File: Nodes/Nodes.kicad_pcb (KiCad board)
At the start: 4 copper layers, 84.8 x 75 mm, 295 parts, among them IC1 VNQ9025AJTR, IC2 VNQ9025AJTR, IC3 TCAN1462VDRQ1, IC4 TCAN1462VDRQ1, IC5 ST730MR, IC6 ST730MR, J1 Conn_01x04, J10 Conn_01x08, J11 Conn_01x08, J12 Conn_01x08, J13 Conn_01x08, J14 Conn_01x08, J2 Conn_01x04, J7 HLE-104-02-L-DV-BE-A-P-TR, J8 HLE-104-02-L-DV-BE-A-P-TR, J9 Conn_01x08, Q1 TN2106K1-G, Q2 TN2106K1-G, SW1 CJS-1201TB1, SW2 CJS-1201TB1, SW3 CAS-220TB1, T1 Conn_01x01, T10 Conn_01x01, T11 Conn_01x01, T12 Conn_01x01, T13 Conn_01x01, T14 Conn_01x01, T15 Conn_01x01, T16 Conn_01x01, T17 Conn_01x01, T18 Conn_01x01, T19 Conn_01x01, T2 Conn_01x01, T20 Conn_01x01, T21 Conn_01x01, T22 Conn_01x01, T23 Conn_01x01, T3 Conn_01x01, T4 Conn_01x01, T5 Conn_01x01, T6 Conn_01x01, T7 Conn_01x01, T8 Conn_01x01, T9 Conn_01x01, U1 STM32G431KBT6, U10 LM358BAIDR, U11 STM32G431RBTx, U5 LM358BAIDR, U6 LM358BAIDR, U7 LM358BAIDR, U8 LM358BAIDR, U9 LM358BAIDR, Y1 SG-8018CE_8.0000M-TJHPA3, Y2 SG-8018CE_8.0000M-TJHPA3

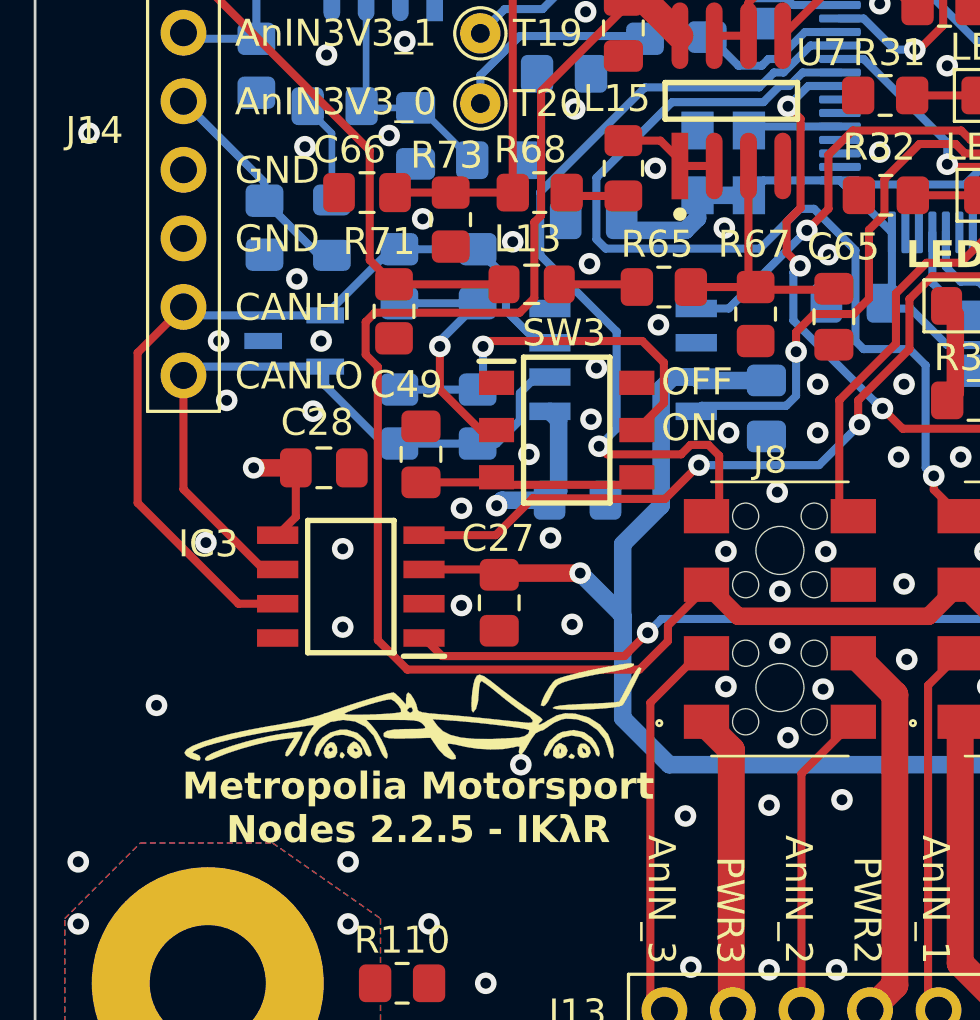
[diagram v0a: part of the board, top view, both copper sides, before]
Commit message: Nodes v2.2.6 Revision 1.1
- CAN connection mistake for Analog Node was fixed
- Updated datasheet about CAN
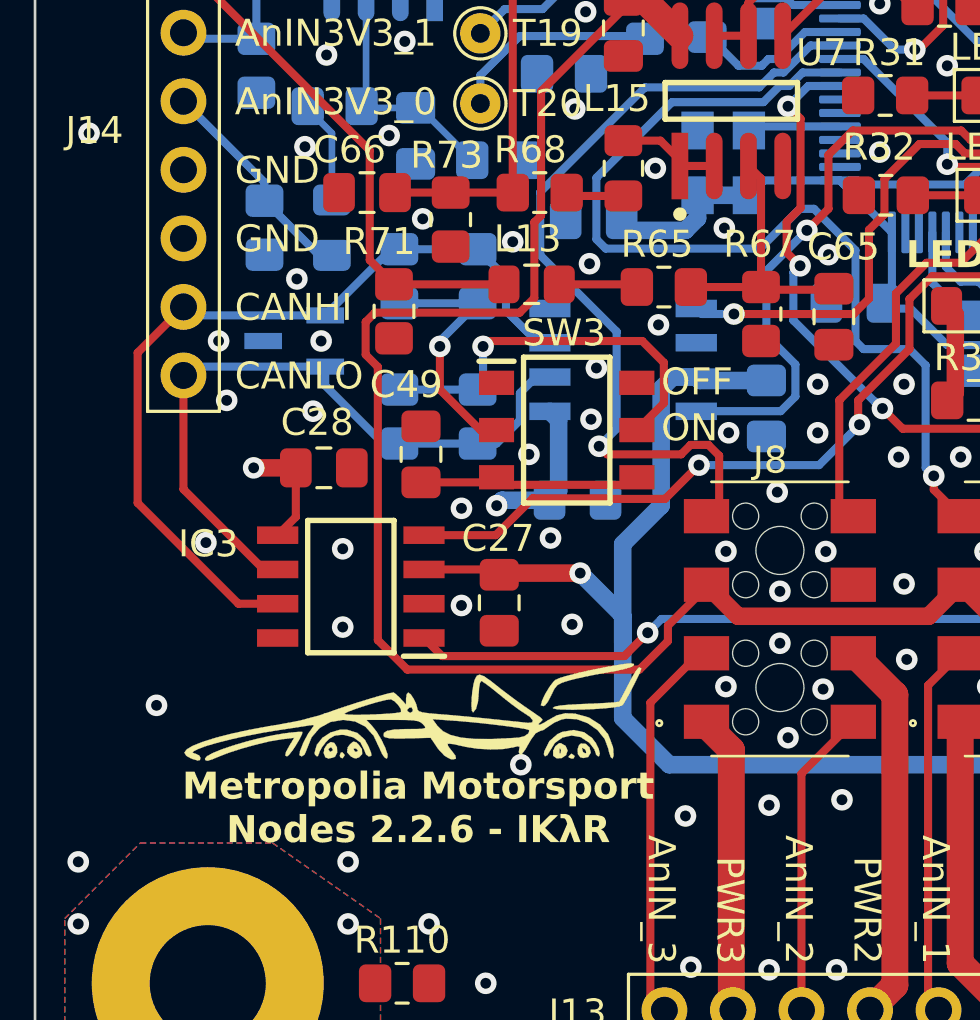
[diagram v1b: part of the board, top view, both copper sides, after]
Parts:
- LED1: value SML-210YTT86M -> SML-210VTT86
- LED10: value SML-H12P8TT86 -> SML-210VTT86
- LED11: value SML-H12D8TT86 -> SML-210VTT86
- LED12: value SML-210VTT86 -> SMLMN2WB1CW1
- LED2, LED6: value SML-210VTT86 -> SML-H12D8TT86
- LED3, LED7: value SMLMN2WB1CW1 -> 150080BS75000
- LED4, LED8: value SMLMN2WB1CW1 -> SML-210YTT86M
- LED5, LED9: value SML-210VTT86 -> SML-H12P8TT86
- moved R67 0.20 mm to (125.4, 111.2)
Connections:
- U11 pad 45: /AnalogNode/CANTx -> /AnalogNode/CANRx
- U11 pad 46: /AnalogNode/CANRx -> /AnalogNode/CANTx
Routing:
- net /AnalogNode/CANRx: track 25.0 -> 26.8 mm
- net /AnalogNode/CANTx: track 21.0 -> 22.2 mm
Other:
- board text added: "Metropolia Motorsport Nodes 2.2.6 - IKλR"
- board text removed: "Metropolia Motorsport Nodes 2.2.5 - IKλR"
